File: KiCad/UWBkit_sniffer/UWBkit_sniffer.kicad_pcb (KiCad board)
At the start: 4 copper layers, 57.4 x 57.4 mm, 81 parts, among them J1 Conn_I2C1, J10 USB_C_Receptacle_USB2.0_14P, J11 USB_C_Receptacle_USB2.0_14P, J2 Conn_I2C2, J3 Conn_01x03, J4 Conn_SPIS, J5 Conn_SPIM, J6 Conn_SWD, J7 Conn_GPIO, J8 Conn_Coaxial, J9 Conn_01x02, SW1 SW_Slide_DPDT, SW2 SW_Push, T1 TestPoint_Small, T10 TestPoint_Small, T11 TestPoint_Small, T12 TestPoint_Small, T2 TestPoint_Small, T3 TestPoint_Small, T4 TestPoint_Small, T5 TestPoint_Small, T6 TestPoint_Small, T7 TestPoint_Small, T8 TestPoint_Small, T9 TestPoint_Small, U1 LBUA5QJ2AB, U2 XC9285B33CMR-G, U3 CP2104, U4 IP4234CZ6, U5 IP4234CZ6

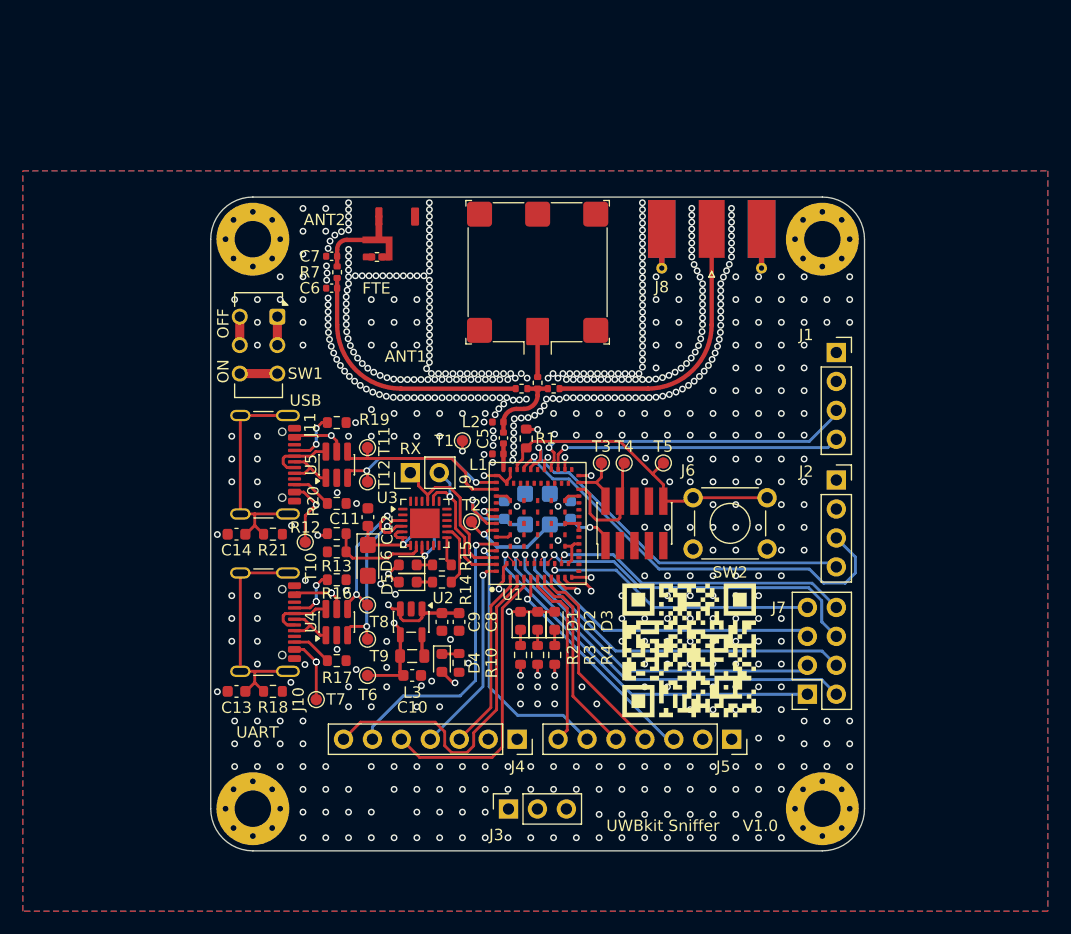
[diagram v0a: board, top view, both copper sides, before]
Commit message: Added connector description
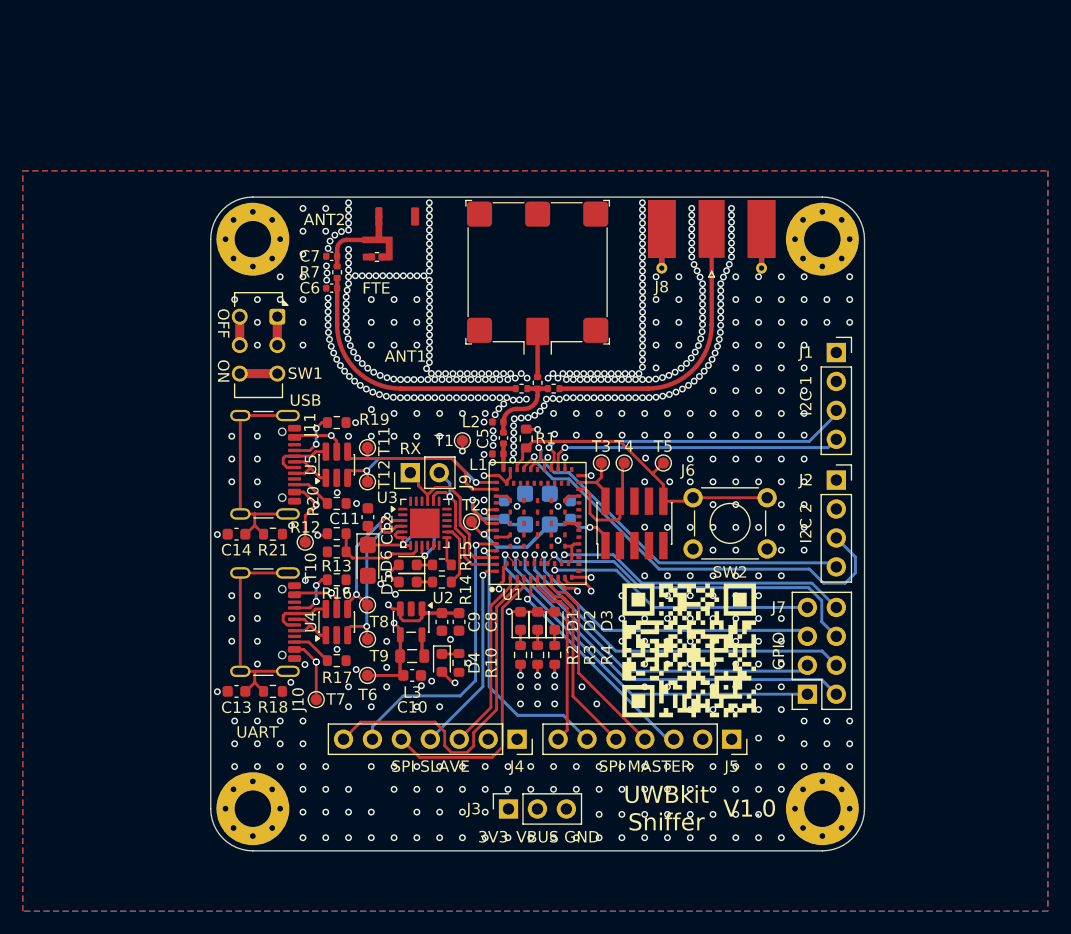
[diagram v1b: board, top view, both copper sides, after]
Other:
- board text added: "3V3"
- board text added: "GND"
- board text added: "GPIO"
- board text added: "I2C 1"
- board text added: "I2C 2"
- board text added: "SPI MASTER"
- board text added: "SPI SLAVE"
- board text added: "VBUS"

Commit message: Removed UWA.01, added CTS/RTS connections
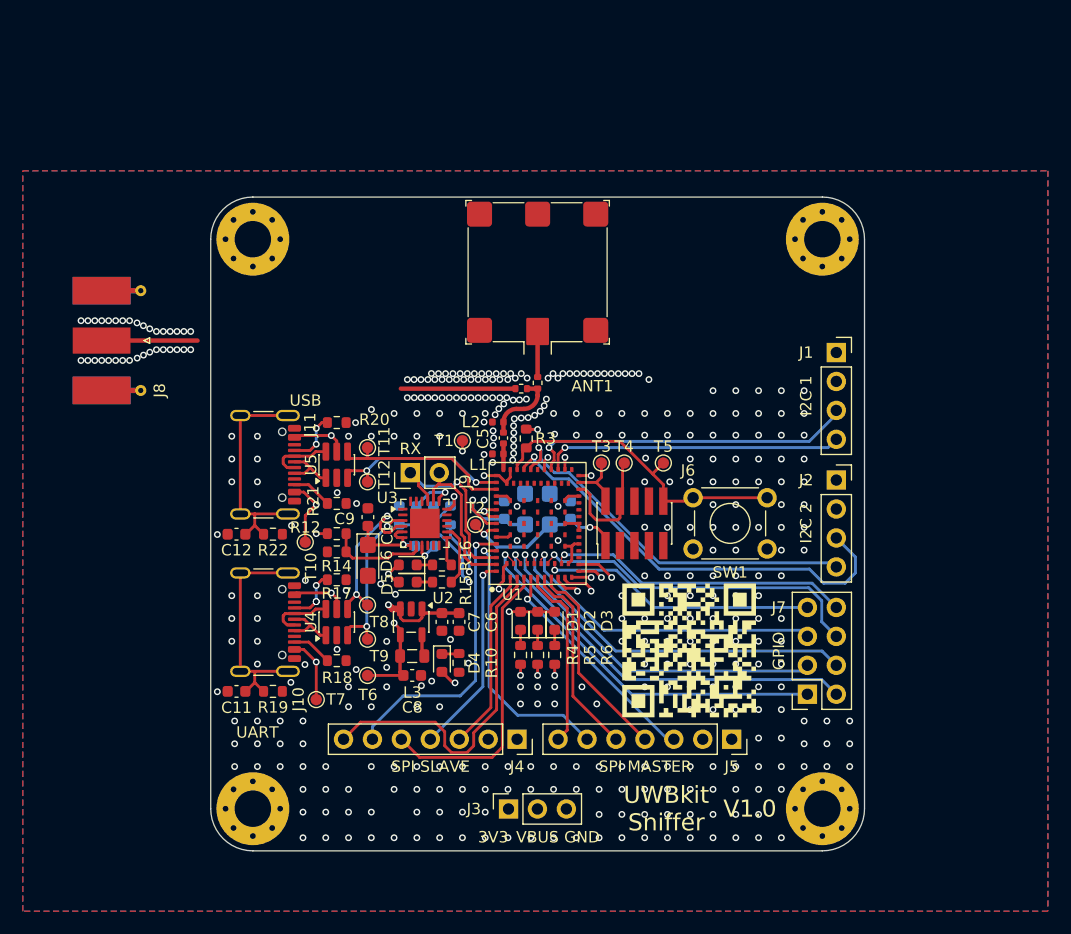
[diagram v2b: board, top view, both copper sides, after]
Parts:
- removed ANT2: Taoglas_UWA.01, UWB_Antennas:Taoglas_UWA.01
- removed the C6 at (142.5, 64.0)
- removed the C7 at (142.5, 61.2)
- removed the R6 at (159.2, 72.8)
- removed the R8 at (146.5, 61.3)
- removed the SW1 at (137.8, 66.5)
- added R1: 0R, Resistor_SMD:R_0603_1608Metric, B.Cu at (152.9, 84.0)
- added R13: 0R, Resistor_SMD:R_0603_1608Metric, B.Cu at (151.4, 84.0)
- added R2: 0R, Resistor_SMD:R_0603_1608Metric, B.Cu at (149.9, 84.0)
- R7: footprint Resistor_SMD:R_0402_1005Metric -> Resistor_SMD:R_0603_1608Metric; moved to B.Cu
- moved J8 52.5 mm to (124.0, 68.6), turned to 0 degrees
- moved R7 22.0 mm to (148.4, 84.0)
- moved R9 2.85 mm to (159.2, 72.8), turned to 180 degrees
- moved R11 2.00 mm to (150.7, 86.7)
- moved T2 0.43 mm to (155.2, 84.8)
- renumbered C12 to C10, C13 to C11, C14 to C12, C8 to C6, C9 to C7, C10 to C8, C11 to C9, R13 to R14, R14 to R15, R15 to R16, R16 to R17, R17 to R18, R18 to R19, R19 to R20, R20 to R21, R21 to R22, R1 to R3, R2 to R4, R3 to R5, R4 to R6, R5 to R8, SW2 to SW1
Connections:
- J10 pad A4: /USB-C_Connector_1/VBUS -> SOC_VBUS
- J10 pad A9: /USB-C_Connector_1/VBUS -> SOC_VBUS
- J10 pad B4: /USB-C_Connector_1/VBUS -> SOC_VBUS
- J10 pad B9: /USB-C_Connector_1/VBUS -> SOC_VBUS
- J11 pad A4: /USB-C_Connector_2/VBUS -> SOC_VBUS
- J11 pad A9: /USB-C_Connector_2/VBUS -> SOC_VBUS
- J11 pad B4: /USB-C_Connector_2/VBUS -> SOC_VBUS
- J11 pad B9: /USB-C_Connector_2/VBUS -> SOC_VBUS
- R7 pad 1: Net-(C6-Pad1) -> /CPU/nCTS
- R7 pad 2: Net-(ANT2-Pad1) -> GND
- T10 pad 1: /USB-C_Connector_2/VBUS -> SOC_VBUS
- T7 pad 1: /USB-C_Connector_1/VBUS -> SOC_VBUS
- U1 pad 12: unconnected-(U1-P1.11-Pad12) -> /CPU/nCTS
- U1 pad 13: unconnected-(U1-P1.10-Pad13) -> /CPU/nRTS
- U3 pad 18: unconnected-(U3-~{CTS}-Pad18) -> /USB2UART/nCTS
- U3 pad 19: unconnected-(U3-~{RTS}-Pad19) -> /USB2UART/nRTS
- U4 pad 5: /USB-C_Connector_1/VBUS -> SOC_VBUS
- U5 pad 5: /USB-C_Connector_2/VBUS -> SOC_VBUS
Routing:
- net /USB-C_Connector_1/VBUS: track 51.2 -> 0.00 mm, vias 4 -> 0
- net /USB-C_Connector_2/VBUS: track 33.1 -> 0.00 mm, vias 2 -> 0
- net /CPU/nCTS: track 0.00 -> 23.6 mm, vias 0 -> 2
- net Net-(C6-Pad1): track 22.8 -> 0.00 mm
- net /CPU/nRTS: track 0.00 -> 21.5 mm, vias 0 -> 2
- net Net-(J8-In): track 24.8 -> 18.5 mm
- net /USB2UART/nCTS: track 0.00 -> 4.76 mm, vias 0 -> 1
- net Net-(ANT2-Pad1): track 4.30 -> 0.00 mm
- net /USB2UART/nRTS: track 0.00 -> 4.07 mm, vias 0 -> 1
- net /CPU/UART_RX: track 14.4 -> 17.2 mm, vias 0 -> 1
- net +3V3: track 165.2 -> 162.7 mm
- net SOC_VBUS: track 112.3 -> 114.3 mm, vias 4 -> 8
- net Net-(U3-~{RST}): track 4.21 -> 2.21 mm
- net /CPU/ANT1: track 7.55 -> 6.65 mm
- net /CPU/UART_TX: track 13.6 -> 13.9 mm, vias 1 -> 0
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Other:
- board text removed: "FTE"
- board text removed: "OFF"
- board text removed: "ON"

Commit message: Redone RF trace, repositioned UWC.20 and mounting holes
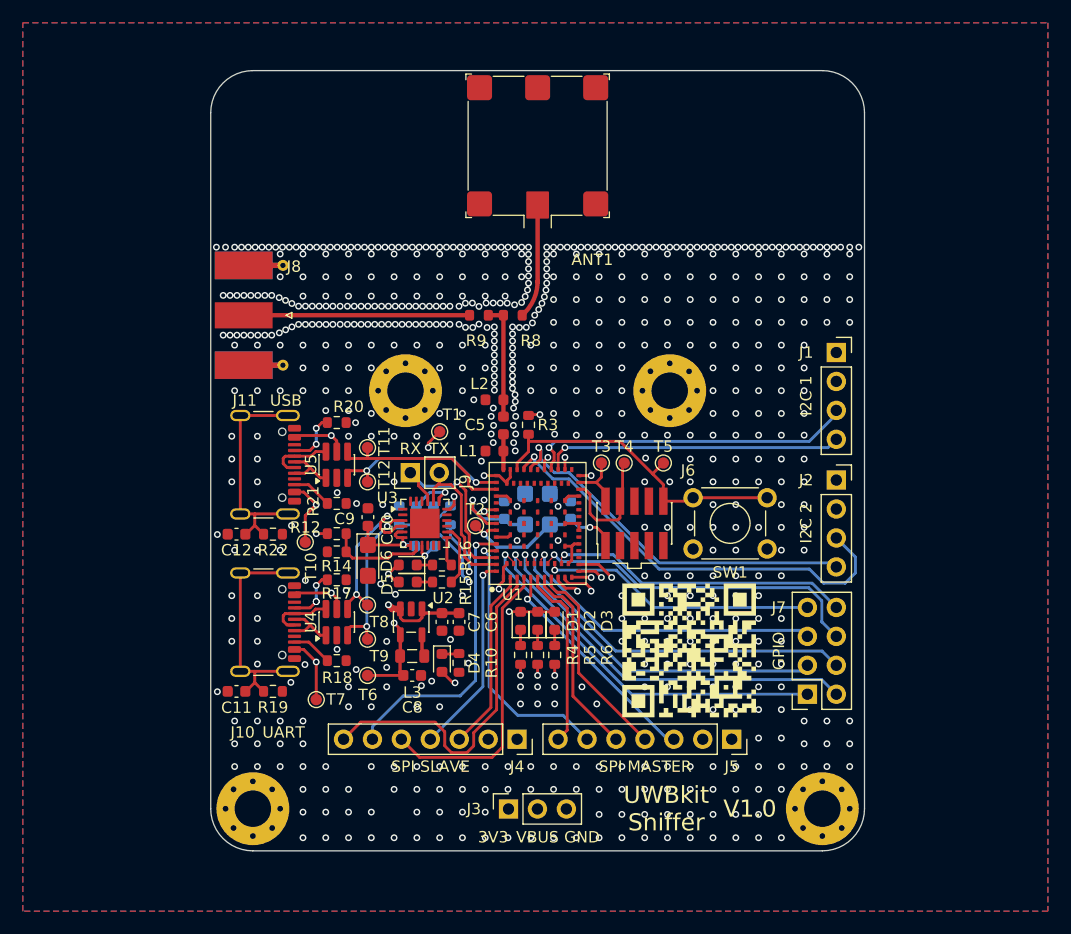
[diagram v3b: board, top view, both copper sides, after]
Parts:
- C5: footprint Capacitor_SMD:C_0402_1005Metric -> Capacitor_SMD:C_0603_1608Metric
- L1, L2: footprint Inductor_SMD:L_0402_1005Metric -> Inductor_SMD:L_0603_1608Metric
- R8, R9: footprint Resistor_SMD:R_0402_1005Metric -> Resistor_SMD:R_0603_1608Metric
- moved H1 18.9 mm to (149.0, 73.0)
- moved H3 18.9 mm to (172.2, 73.0)
- moved J8 12.7 mm to (136.5, 66.4)
- moved ANT1 11.1 mm to (160.6, 51.5)
- moved R9 7.43 mm to (155.4, 66.4)
- moved R8 6.32 mm to (158.4, 66.4), turned to 0 degrees
- moved T1 2.15 mm to (152.0, 76.6)
- moved L2 1.98 mm to (156.8, 73.8)
- moved R3 1.22 mm to (159.8, 76.0)
- moved C5 1.10 mm to (157.6, 76.0)
- moved L1 0.40 mm to (156.8, 78.3)
- moved T2 0.10 mm to (155.2, 84.9)
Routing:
- net Net-(ANT1-Pad1): track 4.00 -> 10.1 mm
- net /CPU/ANT1: track 6.65 -> 10.2 mm
- net Net-(J8-In): track 18.5 -> 19.8 mm
- net +3V3: track 162.7 -> 164.0 mm
- net /CPU/nRST: track 28.1 -> 29.0 mm
- net Net-(U1-ANT1): track 2.30 -> 3.10 mm
- net SOC_VBUS: track 114.3 -> 114.9 mm
- net GND: vias 399 -> 655
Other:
- board size 57.4 x 57.4 mm -> 57.4 x 68.5 mm
- board text added: "TX"

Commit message: Improved placement of ICs and ports and the board is now smaller
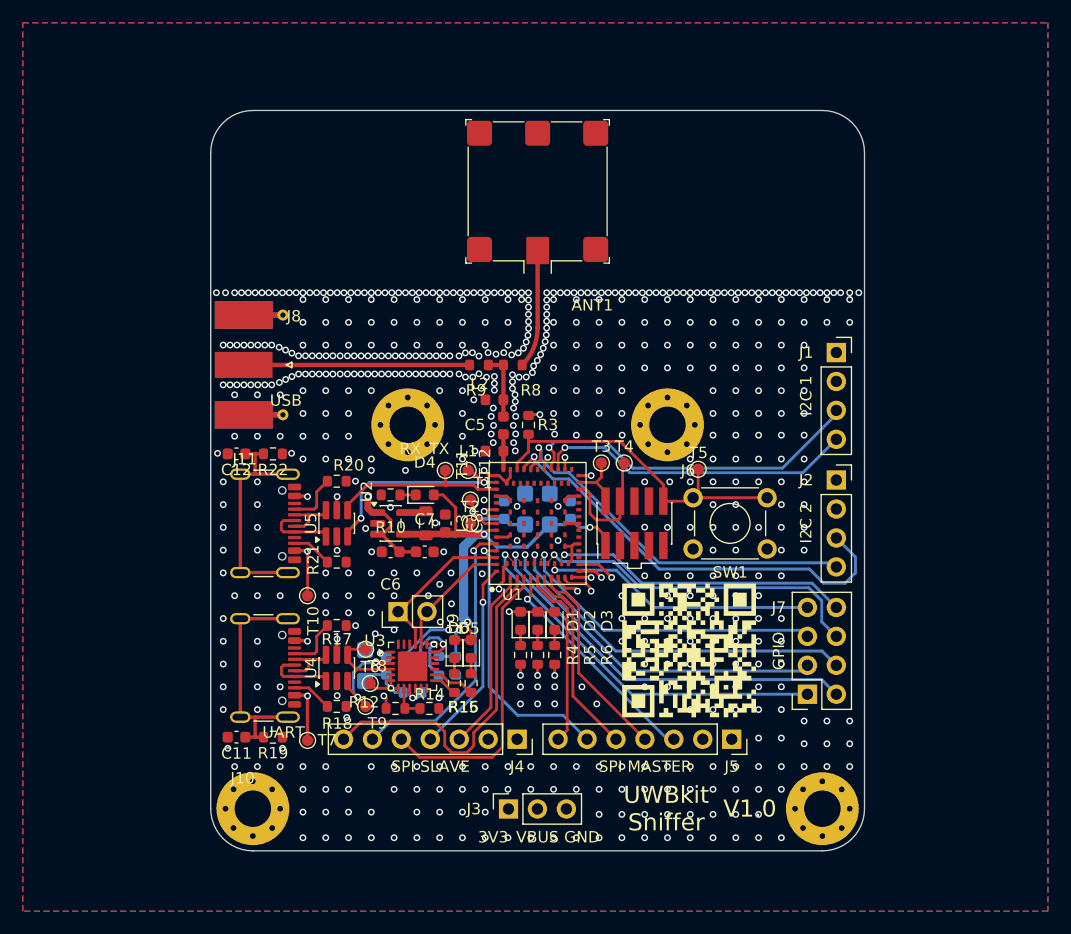
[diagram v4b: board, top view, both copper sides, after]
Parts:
- C10, C9: moved to B.Cu
- moved R12 16.2 mm to (148.1, 100.9)
- moved R14 16.0 mm to (151.1, 100.9), turned to 0 degrees
- moved R10 15.9 mm to (147.7, 82.2), turned to 180 degrees
- moved D4 14.8 mm to (150.7, 82.2), turned to 0 degrees
- moved R7 14.1 mm to (153.4, 97.2), turned to -90 degrees
- moved R1 13.8 mm to (148.9, 97.2), turned to 90 degrees
- moved C8 13.7 mm to (152.5, 84.7), turned to 90 degrees
- moved R2 13.3 mm to (151.9, 97.2), turned to 90 degrees
- moved R13 13.2 mm to (150.3, 97.2), turned to -90 degrees
- moved C9 13.1 mm to (147.3, 97.2)
- moved R11 12.9 mm to (149.6, 99.5)
- moved U3 12.6 mm to (149.6, 97.2)
- moved J9 12.2 mm to (148.3, 92.4)
- moved L3 11.7 mm to (150.8, 84.7), turned to -90 degrees
- moved R16 10.4 mm to (153.3, 98.7), turned to -90 degrees
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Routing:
- net SOC_VBUS: track 114.9 -> 104.3 mm, vias 8 -> 9
- net /USB2UART_D-: track 14.6 -> 6.53 mm, vias 2 -> 0
- net /USB2UART_D+: track 14.6 -> 8.90 mm
- net Net-(U3-VBUS): track 8.72 -> 3.12 mm
- net +3V3: track 164.0 -> 159.3 mm, vias 9 -> 7
- net /CPU/nRTS: track 21.5 -> 25.9 mm
- net /CPU/ANT1: track 10.2 -> 5.86 mm
- net /CPU/UART_RX: track 17.2 -> 14.0 mm, vias 1 -> 0
- net /CPU/UART_TX: track 13.9 -> 10.9 mm
- net /SOC_D+: track 15.8 -> 18.5 mm
- net /USB2UART/nCTS: track 4.76 -> 7.10 mm
- net /CPU/nCTS: track 23.6 -> 21.7 mm
- net /CPU/I2C1_SCL: track 29.0 -> 30.9 mm
- net /CPU/I2C1_SDA: track 26.3 -> 28.1 mm
- net Net-(U3-TXT/GPIO.0): track 5.44 -> 3.84 mm
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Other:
- board size 57.4 x 68.5 mm -> 57.4 x 65 mm

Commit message: Moved silkscreen text to be more visible
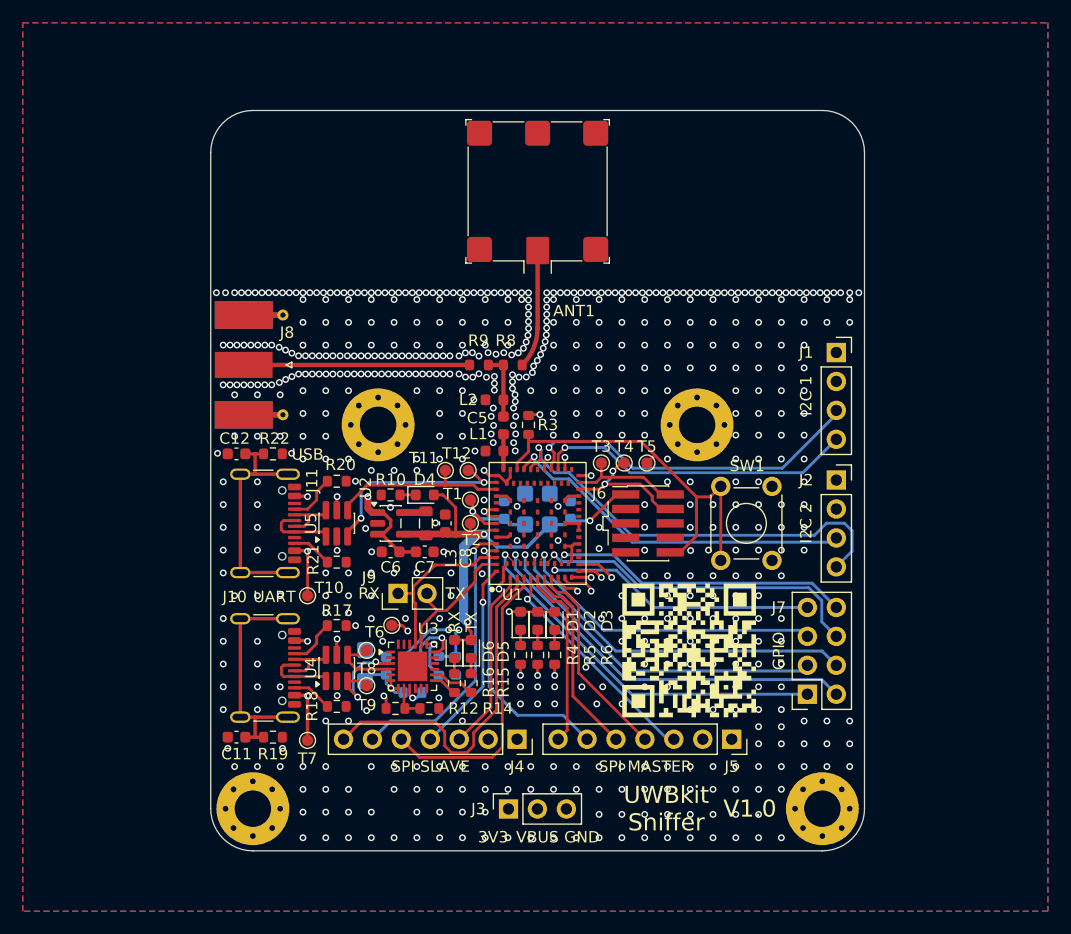
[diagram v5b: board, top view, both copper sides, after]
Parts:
- moved SW1 5.52 mm to (181.2, 81.4), turned to -90 degrees
- moved T6 5.44 mm to (147.8, 93.6)
- moved T5 4.53 mm to (170.2, 79.3)
- moved H1 2.60 mm to (146.6, 76.0)
- moved H3 2.60 mm to (174.6, 76.0)
- moved T9 1.82 mm to (145.6, 98.9)
- moved J9 1.60 mm to (148.3, 90.8)
- moved J6 1.19 mm to (170.3, 84.7), turned to 0 degrees
- moved T8 0.14 mm to (145.6, 95.8)
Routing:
- net /CPU/I2C2_SCL: track 38.6 -> 31.5 mm
- net +3V3: track 159.3 -> 165.9 mm, vias 7 -> 8
- net /CPU/nRST: track 30.3 -> 36.6 mm
- net /CPU/SWDIO: track 5.40 -> 10.1 mm
- net /CPU/I2C2_SDA: track 33.4 -> 38.1 mm
- net /CPU/UART_TX: track 10.9 -> 12.8 mm
- net /CPU/SWCLK: track 10.8 -> 12.1 mm, vias 0 -> 2
- net /CPU/UART_RX: track 14.0 -> 14.8 mm
- net /USB2UART_D+: track 8.90 -> 9.64 mm
- net GND: vias 602 -> 614
